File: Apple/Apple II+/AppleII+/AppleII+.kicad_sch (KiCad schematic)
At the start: 0 parts

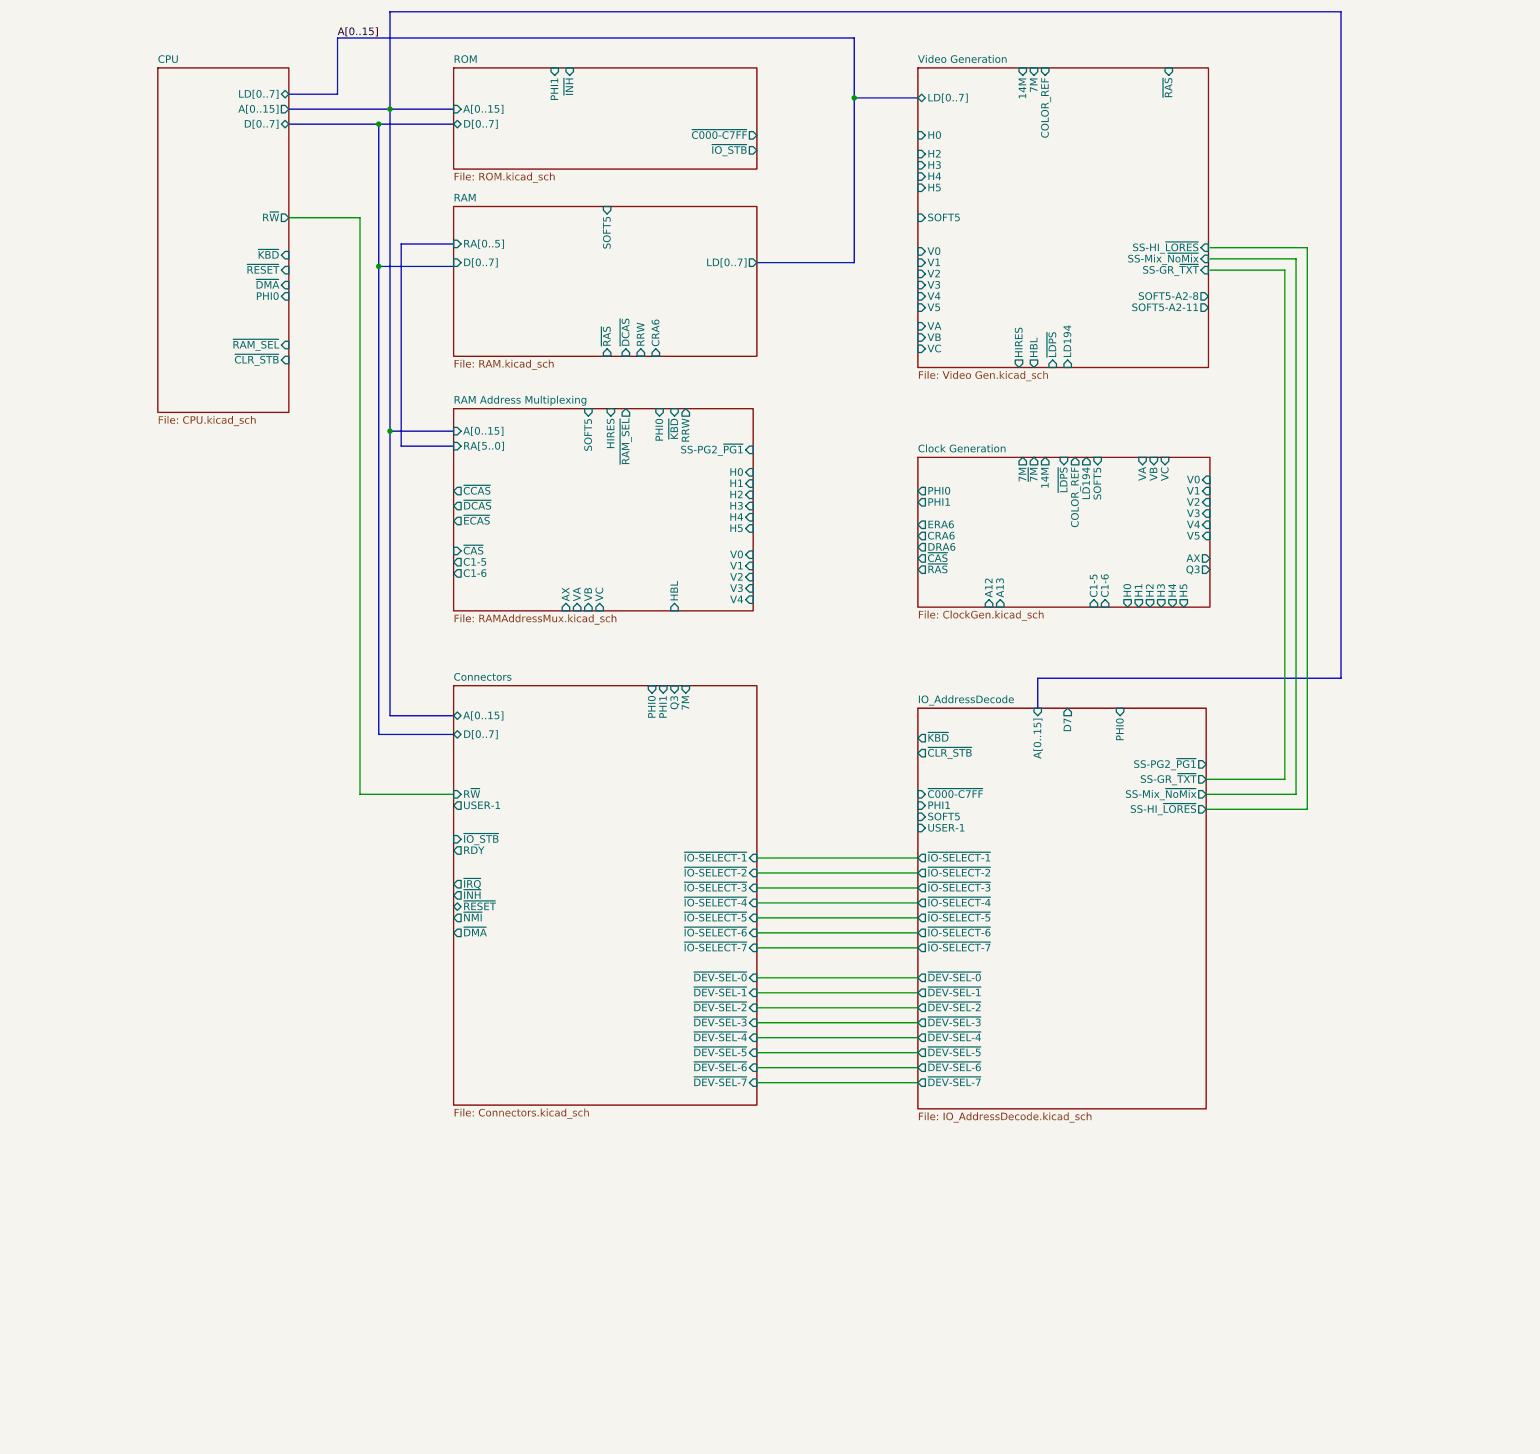
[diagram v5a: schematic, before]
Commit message: Fixed CAS and A6 on RAM page (plus lots of other clean ups)
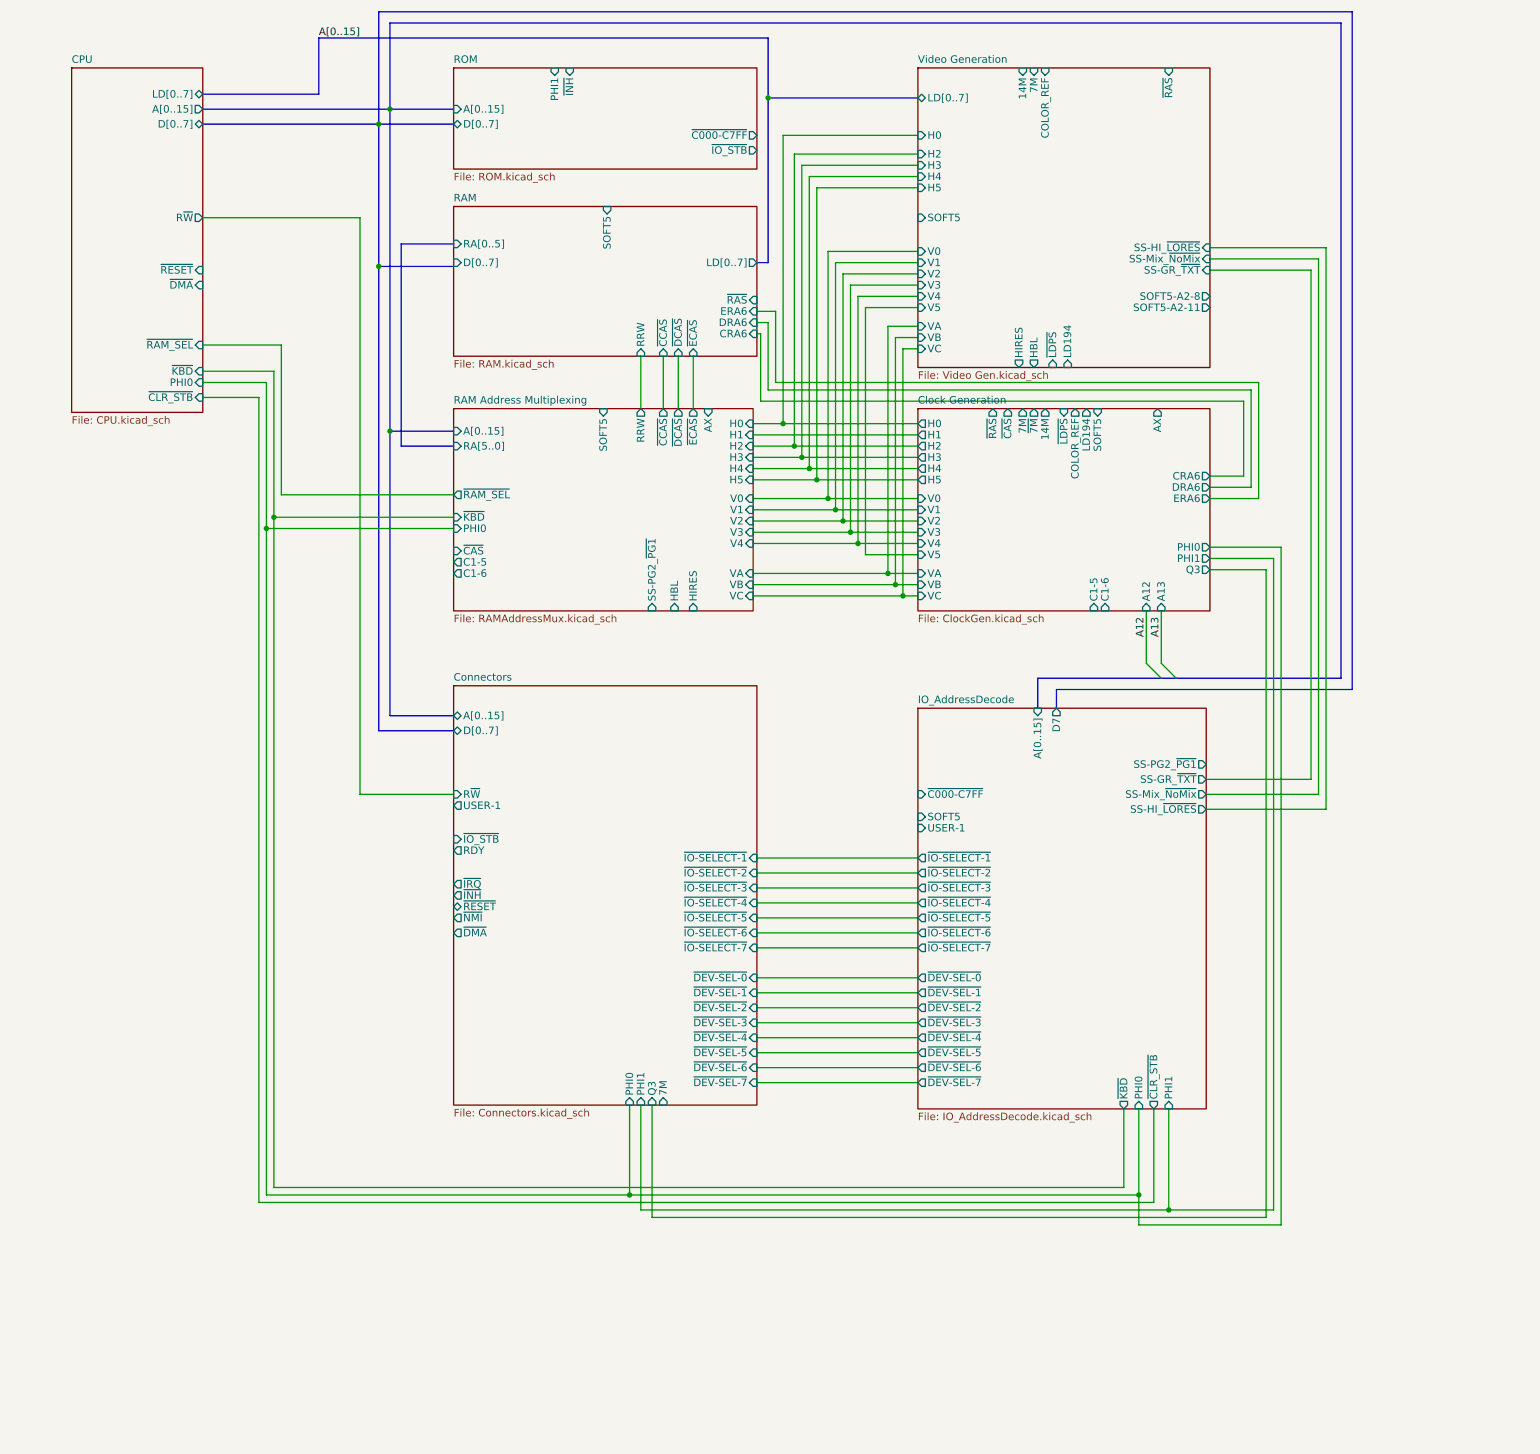
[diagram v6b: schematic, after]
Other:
- sheet RAM ports: added DRA6, ERA6, ~{CCAS}, ~{ECAS}; removed none

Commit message: first time re-running ERC
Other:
- sheet CPU ports: added ~{IRQ}, ~{NMI}, ~{RDY}; removed none
